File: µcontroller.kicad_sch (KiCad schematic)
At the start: 15 parts, among them U2 stm32G4

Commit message: Can aangesloten
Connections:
- net CAN_RX: now reaches U2.45 (PA11)
- net CAN_TX: now reaches U2.46 (PA12)
- net CAN_STB: now reaches U2.49 (PA13)
- net CAN_SHDN: now reaches U2.50 (PA14)
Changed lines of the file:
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@@
+	(wire
+		(pts
+			(xy 154.94 85.09) (xy 158.75 85.09)
+		)
+		(stroke
+			(width 0)
+			(type default)
+		)
+	)
 	(wire
 		(pts
@@
 	(wire
 		(pts
+			(xy 154.94 82.55) (xy 158.75 82.55)
+		)
+		(stroke
+			(width 0)
+			(type default)
+		)
+	)
+	(wire
+		(pts
 			(xy 137.16 35.56) (xy 142.24 35.56)
 		)
@@
 	(wire
 		(pts
+			(xy 154.94 80.01) (xy 158.75 80.01)
+		)
+		(stroke
+			(width 0)
+			(type default)
+		)
+	)
+	(wire
+		(pts
 			(xy 171.45 43.18) (xy 182.88 43.18)
 		)
@@
 		(pts
 			(xy 134.62 35.56) (xy 137.16 35.56)
+		)
+		(stroke
+			(width 0)
+			(type default)
+		)
+	)
+	(wire
+		(pts
+			(xy 154.94 87.63) (xy 158.75 87.63)
 		)
 		(stroke
@@
 		)
 	)
+	(hierarchical_label "CAN_STB"
+		(shape output)
+		(at 158.75 85.09 0)
+		(effects
+			(font
+				(size 1.27 1.27)
+			)
+			(justify left)
+		)
+	)
 	(hierarchical_label "QSPI_IO3"
 		(shape bidirectional)
@@
 		)
 	)
+	(hierarchical_label "CAN_SHDN"
+		(shape output)
+		(at 158.75 87.63 0)
+		(effects
+			(font
+				(size 1.27 1.27)
+			)
+			(justify left)
+		)
+	)
 	(hierarchical_label "QSPI_IO2"
 		(shape bidirectional)
@@
 		(effects
 			(font
+				(size 1.27 1.27)
+			)
+			(justify left)
+		)
+	)
+	(hierarchical_label "CAN_RX"
+		(shape input)
+		(at 158.75 80.01 0)
+		(effects
+			(font
+				(size 1.27 1.27)
+			)
+			(justify left)
+		)
+	)
+	(hierarchical_label "CAN_TX"
+		(shape output)
+		(at 158.75 82.55 0)
+		(effects
+			(font

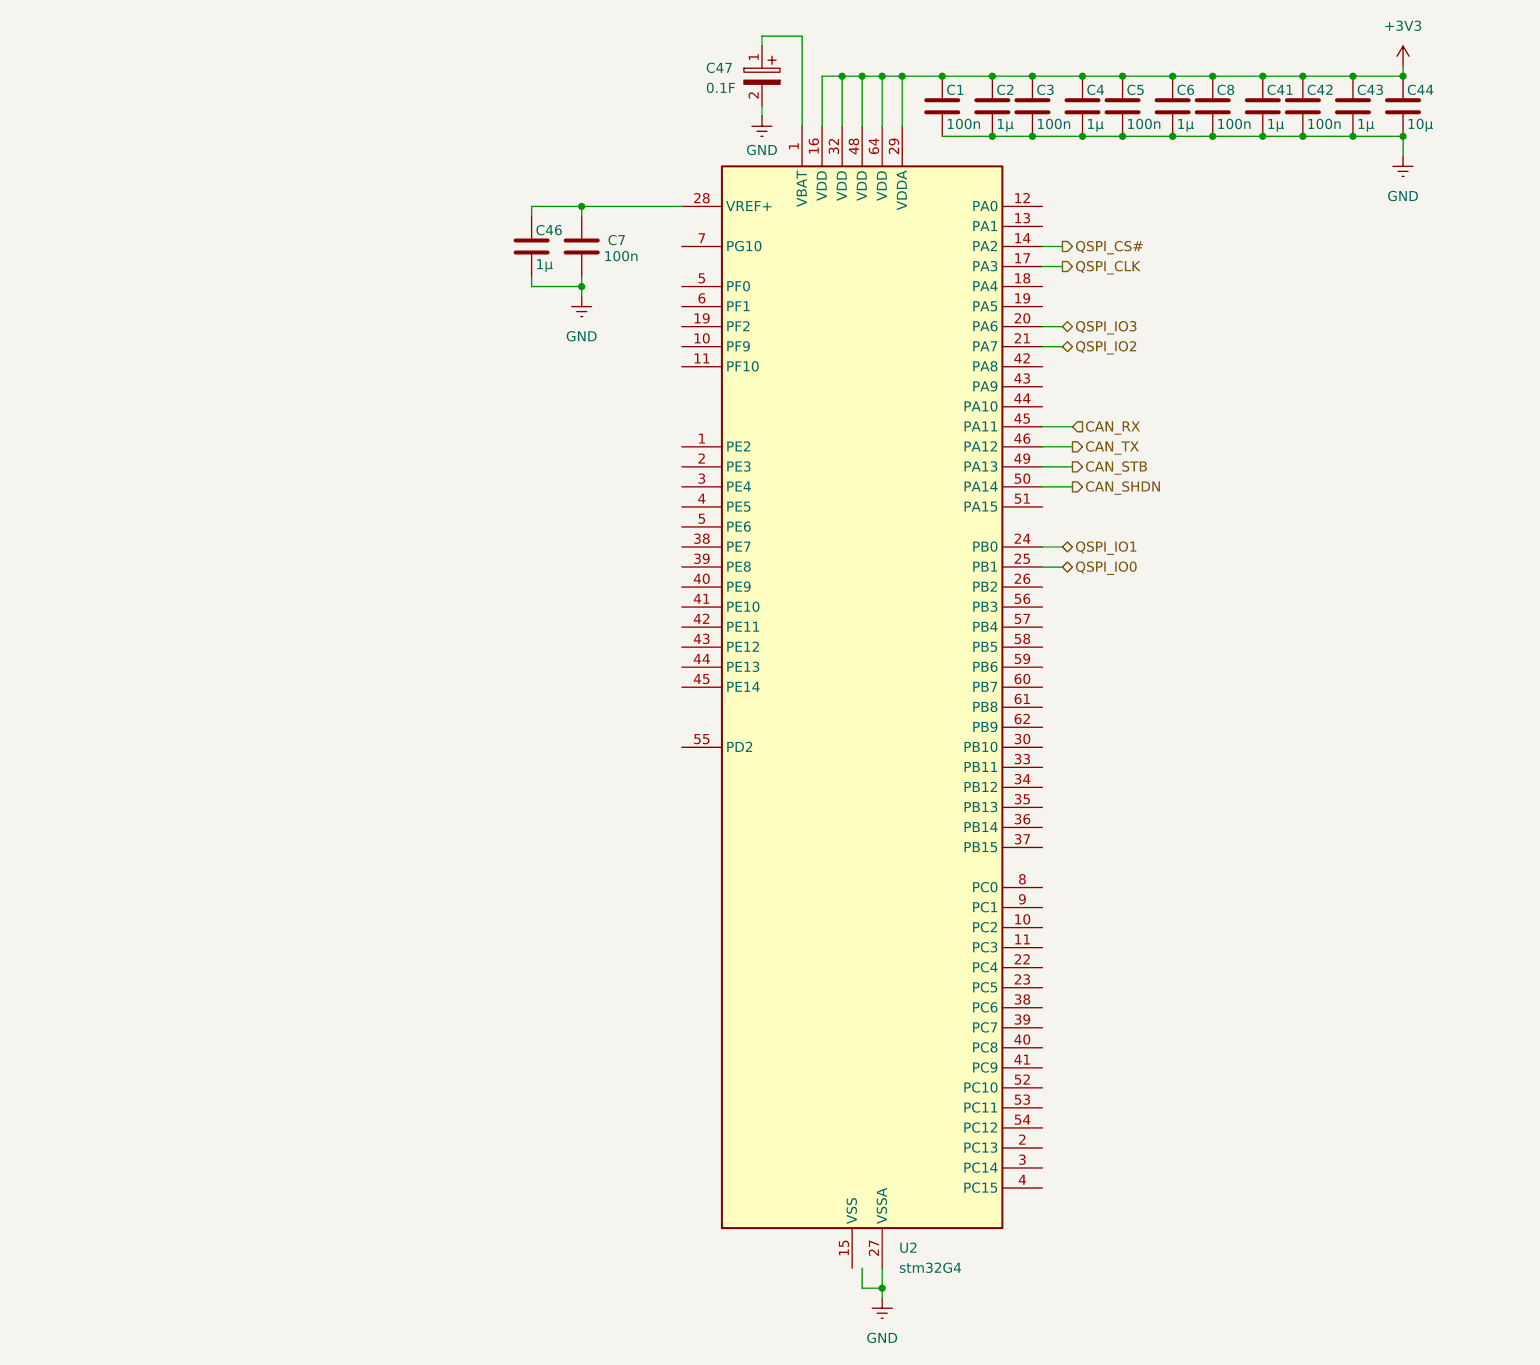
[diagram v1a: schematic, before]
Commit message: footprints
footprints aan de condensators toegevoegd
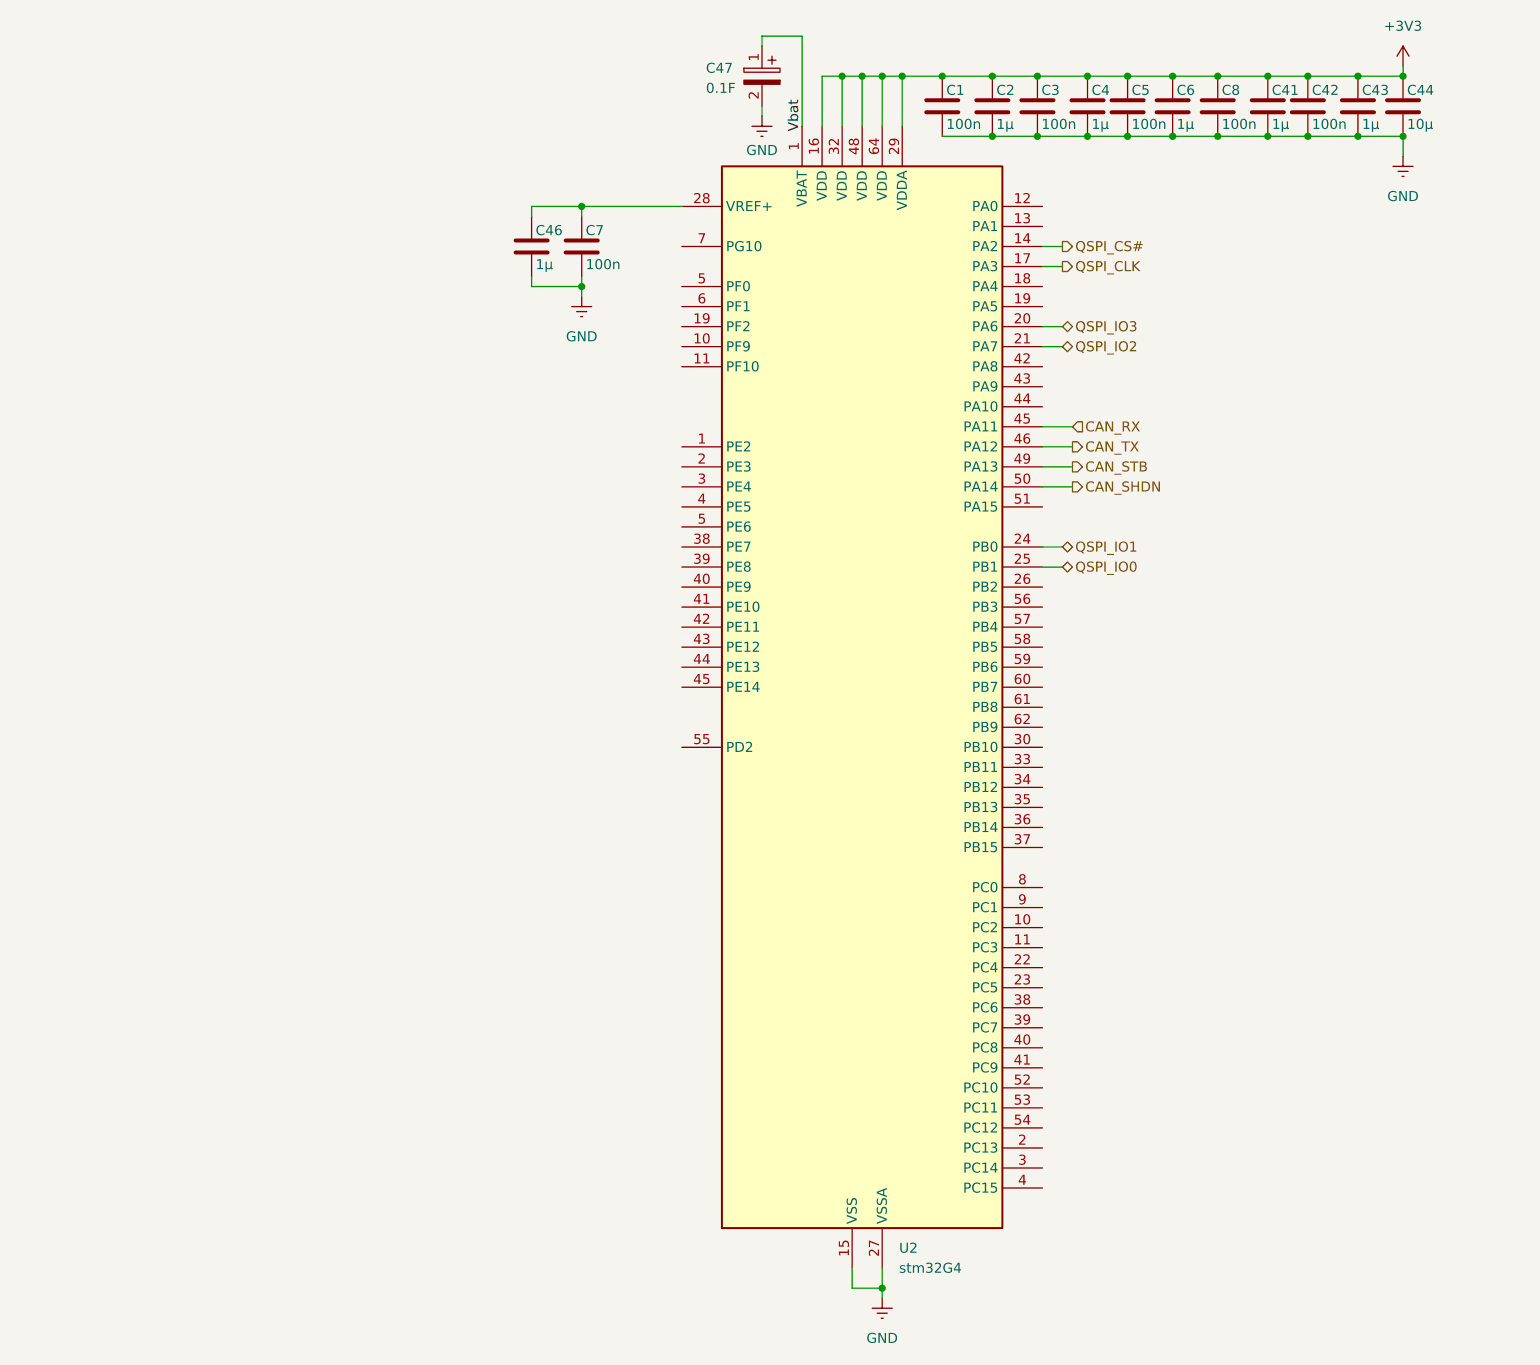
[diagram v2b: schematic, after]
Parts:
- C1, C2, C3, C4, C41, C42, C43, C44, C46, C5, C6, C7, C8: footprint (none) -> Capacitor_SMD:C_0603_1608Metric
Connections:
- net VSS is gone; now on net GND: U2.15 (VSS), U2.31 (VSS), U2.47 (VSS), U2.63 (VSS)

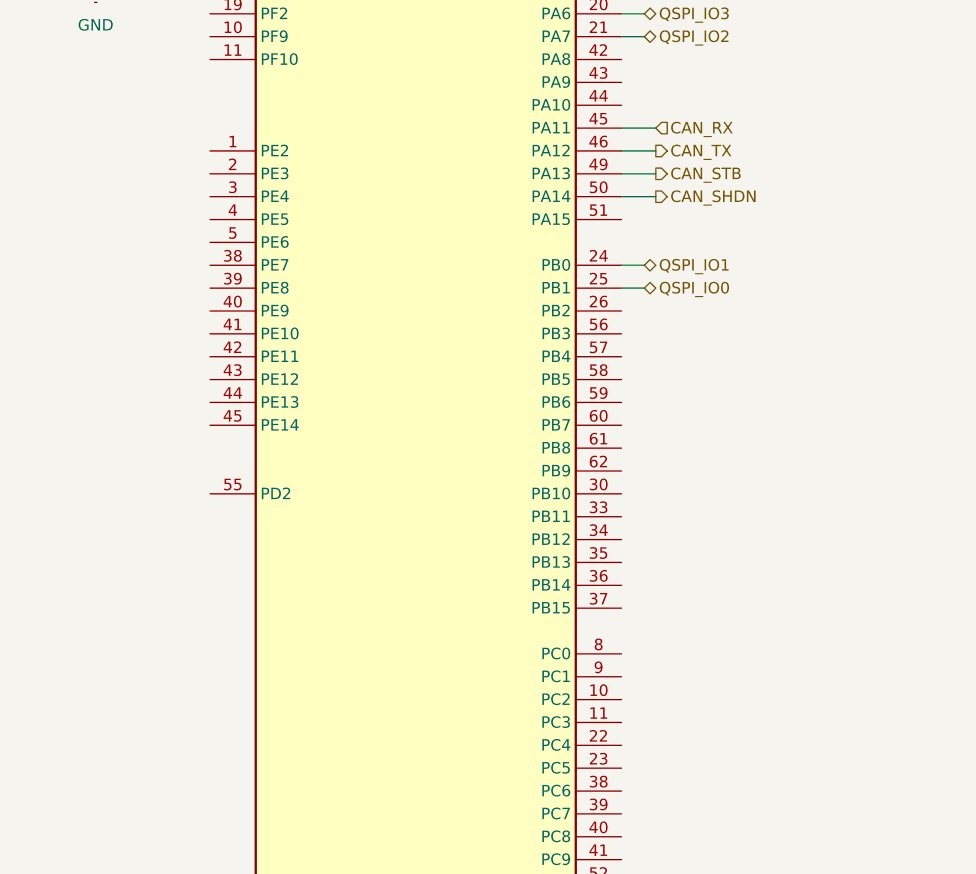
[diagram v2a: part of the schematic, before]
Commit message: BLDC en 5V
bldc motor aangesloten alsook 5V gemaakt
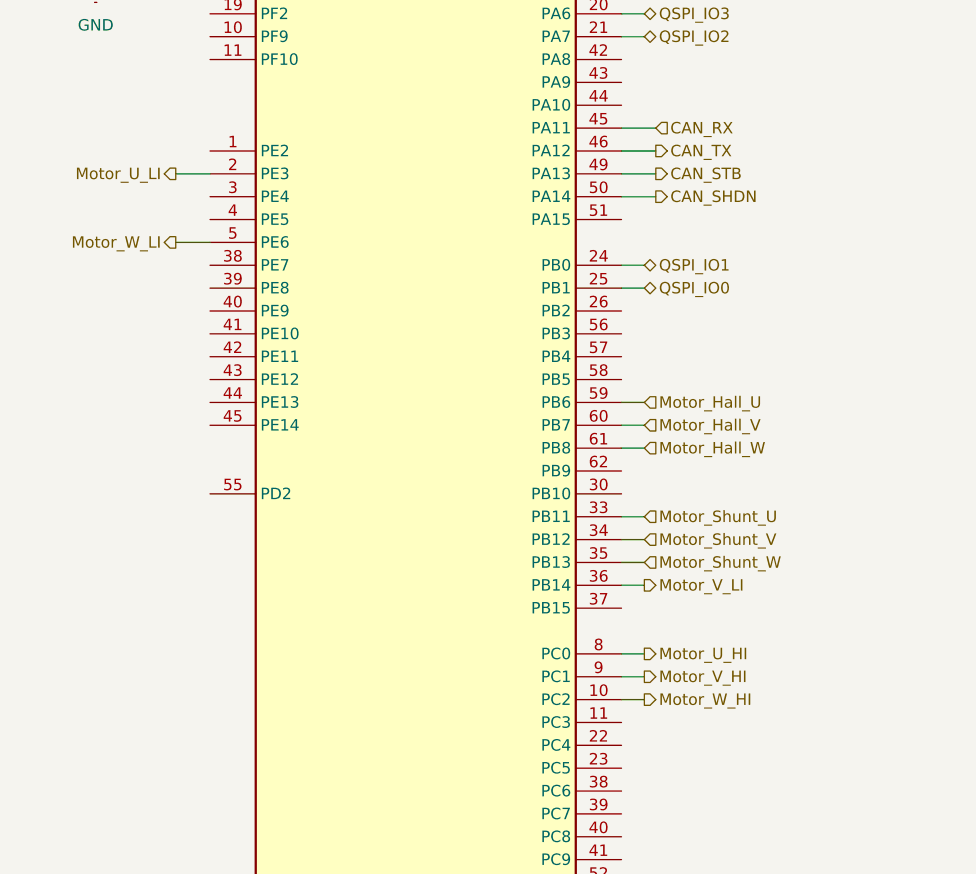
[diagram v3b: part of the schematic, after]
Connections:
- net Motor_W_HI: now reaches U2.10 (PC2)
- net Motor_U_LI: now reaches U2.2 (PC13)
- net Motor_Shunt_U: now reaches U2.33 (PB11)
- net Motor_Shunt_V: now reaches U2.34 (PB12)
- net Motor_Shunt_W: now reaches U2.35 (PB13)
- net Motor_V_LI: now reaches U2.36 (PB14)
- net Motor_W_LI: now reaches U2.5 (PE6)
- net Motor_Hall_U: now reaches U2.59 (PB6)
- net Motor_Hall_V: now reaches U2.60 (PB7)
- net Motor_Hall_W: now reaches U2.61 (PB8)
- net Motor_U_HI: now reaches U2.8 (PC0)
- net Motor_V_HI: now reaches U2.9 (PC1)
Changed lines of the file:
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@@
+	(wire
+		(pts
+			(xy 154.94 143.51) (xy 157.48 143.51)
+		)
+		(stroke
+			(width 0)
+			(type default)
+		)
+	)
 	(wire
 		(pts
@@
 	(wire
 		(pts
+			(xy 154.94 130.81) (xy 157.48 130.81)
+		)
+		(stroke
+			(width 0)
+			(type default)
+		)
+	)
+	(wire
+		(pts
 			(xy 90.17 62.23) (xy 96.52 62.23)
 		)
@@
 	(wire
 		(pts
+			(xy 154.94 125.73) (xy 157.48 125.73)
+		)
+		(stroke
+			(width 0)
+			(type default)
+		)
+	)
+	(wire
+		(pts
 			(xy 96.52 52.07) (xy 96.52 53.34)
 		)
@@
 	(wire
 		(pts
+			(xy 154.94 113.03) (xy 157.48 113.03)
+		)
+		(stroke
+			(width 0)
+			(type default)
+		)
+	)
+	(wire
+		(pts
 			(xy 130.81 186.69) (xy 130.81 189.23)
 		)
@@
 	(wire
 		(pts
+			(xy 105.41 85.09) (xy 109.22 85.09)
+		)
+		(stroke
+			(width 0)
+			(type default)
+		)
+	)
+	(wire
+		(pts
 			(xy 188.595 35.56) (xy 194.945 35.56)
 		)
@@
 	(wire
 		(pts
+			(xy 154.94 115.57) (xy 157.48 115.57)
+		)
+		(stroke
+			(width 0)
+			(type default)
+		)
+	)
+	(wire
+		(pts
 			(xy 160.655 43.18) (xy 165.735 43.18)
 		)
@@
 	(wire
 		(pts
+			(xy 105.41 92.71) (xy 109.22 92.71)
+		)
+		(stroke
+			(width 0)
+			(type default)
+		)
+	)
+	(wire
+		(pts
 			(xy 90.17 60.96) (xy 90.17 62.23)
 		)
@@
 	(wire
 		(pts
+			(xy 154.94 123.19) (xy 157.48 123.19)
+		)
+		(stroke
+			(width 0)
+			(type default)
+		)
+	)
+	(wire
+		(pts
 			(xy 154.94 57.15) (xy 157.48 57.15)
 		)
@@
 	(wire
 		(pts
+			(xy 154.94 110.49) (xy 157.48 110.49)
+		)
+		(stroke
+			(width 0)
+			(type default)
+		)
+	)
+	(wire
+		(pts
 			(xy 154.305 35.56) (xy 160.655 35.56)
 		)
@@
 	(wire
 		(pts
+			(xy 154.94 140.97) (xy 157.48 140.97)
+		)
+		(stroke
+			(width 0)
+			(type default)
+		)
+	)
+	(wire
+		(pts
 			(xy 154.94 69.85) (xy 157.48 69.85)
 		)
@@
 	(wire
 		(pts
+			(xy 154.94 128.27) (xy 157.48 128.27)
+		)
+		(stroke
+			(width 0)
+			(type default)
+		)
+	)
+	(wire
+		(pts
 			(xy 148.59 35.56) (xy 154.305 35.56)
 		)
@@
 		(pts
 			(xy 96.52 52.07) (xy 90.17 52.07)
+		)
+		(stroke
+			(width 0)
+			(type default)
+		)
+	)
+	(wire
+		(pts
+			(xy 154.94 138.43) (xy 157.48 138.43)
 		)
 		(stroke
@@
 		)
 	)
+	(hierarchical_label "Motor_V_HI"
+		(shape output)
+		(at 157.48 140.97 0)
+		(effects
+			(font
+				(size 1.27 1.27)
+			)
+			(justify left)
+		)
+	)
 	(hierarchical_label "QSPI_CS#"
 		(shape output)
@@
 		(shape output)
 		(at 158.75 85.09 0)
+		(effects
+			(font
+				(size 1.27 1.27)
+			)
+			(justify left)
+		)
+	)
+	(hierarchical_label "Motor_W_LI"
+		(shape output)
+		(at 105.41 92.71 180)
+		(effects
+			(font
+				(size 1.27 1.27)
+			)
+			(justify right)
+		)
+	)
+	(hierarchical_label "Motor_Shunt_U"
+		(shape input)
+		(at 157.48 123.19 0)
 		(effects
 			(font
@@
 		)
 	)
+	(hierarchical_label "Motor_U_HI"
+		(shape output)
+		(at 157.48 138.43 0)
+		(effects
+			(font
+				(size 1.27 1.27)
+			)
+			(justify left)
+		)
+	)
 	(hierarchical_label "CAN_SHDN"
 		(shape output)
 		(at 158.75 87.63 0)
+		(effects
+			(font
+				(size 1.27 1.27)
+			)
+			(justify left)
+		)
+	)
+	(hierarchical_label "Motor_W_HI"
+		(shape output)
+		(at 157.48 143.51 0)
 		(effects
 			(font
@@
 		)
 	)
+	(hierarchical_label "Motor_Hall_W"
+		(shape input)
+		(at 157.48 115.57 0)
+		(effects
+			(font
+				(size 1.27 1.27)
+			)
+			(justify left)
+		)
+	)
 	(hierarchical_label "QSPI_IO0"
 		(shape bidirectional)
@@
 		)
 	)
+	(hierarchical_label "Motor_U_LI"
+		(shape output)
+		(at 105.41 85.09 180)
+		(effects
+			(font
+				(size 1.27 1.27)
+			)
+			(justify right)
+		)
+	)
+	(hierarchical_label "Motor_Hall_U"
+		(shape input)
+		(at 157.48 110.49 0)
+		(effects
+			(font
+				(size 1.27 1.27)
+			)
+			(justify left)
+		)
+	)
+	(hierarchical_label "Motor_Shunt_W"
+		(shape input)
+		(at 157.48 128.27 0)
+		(effects
+			(font
+				(size 1.27 1.27)
+			)
+			(justify left)
+		)
+	)
 	(hierarchical_label "CAN_RX"
 		(shape input)
@@
 		)
 	)
+	(hierarchical_label "Motor_V_LI"
+		(shape output)
+		(at 157.48 130.81 0)
+		(effects
+			(font
+				(size 1.27 1.27)
+			)
+			(justify left)
+		)
+	)
+	(hierarchical_label "Motor_Hall_V"
+		(shape input)
+		(at 157.48 113.03 0)
+		(effects
+			(font
+				(size 1.27 1.27)
+			)
+			(justify left)
+		)
+	)
 	(hierarchical_label "CAN_TX"
 		(shape output)
@@
 		(effects
 			(font
+				(size 1.27 1.27)
+			)
+			(justify left)
+		)
+	)
+	(hierarchical_label "Motor_Shunt_V"
+		(shape input)
+		(at 157.48 125.73 0)
+		(effects
+			(font

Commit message: schemas klaar
schemas en footprints aan symbolen allemaal juist gemaakt
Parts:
- removed C47: 0.1F, Condensator_Polarized:RSCVS1043R6G08012T, symbol Condensator_Polarized:RSCVS1043R6G08012T
- added C3: (no value), Footprintsymbolen_samen:SuperCap 0.1F 10.5mmx10.8mm, symbol Schemasymbolen_samen:SuperCap_0.1F
- U1: renamed from U2; footprint STM32G4:STM32G474 -> Footprintsymbolen_samen:STM32G474
- renumbered C46 to C1, C8 to C10, C41 to C11, C42 to C12, C43 to C13, C44 to C14, C7 to C2, C1 to C4, C2 to C5, C3 to C6, C4 to C7, C5 to C8, C6 to C9
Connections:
- net GND: now also C3.2
- net Motor_Shunt_U: now also U1.13 (PA1); no longer U1.33 (PB11)
- net Motor_Shunt_V: now also U1.33 (PB11); no longer U1.34 (PB12)
- net Motor_Shunt_W: now also U1.34 (PB12); no longer U1.35 (PB13)
- net Motor_U_LI: now also U1.35 (PB13); no longer U1.2 (PC13)
- net Motor_W_LI: now also U1.37 (PB15); no longer U1.5 (PE6)
- new net: C3.1, U1.1 (VBAT)
